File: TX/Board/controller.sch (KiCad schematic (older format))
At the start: 12 parts, among them J1 CONN_SWITCH, J2 PROG_CONN, J3 RX_JMP, J4 TX_JMP, J5 AT_MODE_JUMP, J6 BATT_CONN, J7 GENERIC, U1 ARDUINO_PRO_MINI, U2 ITEAD_HC-05

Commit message: Corrected bugs and added first prototype of receiver board
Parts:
- added R1: R, Resistors_THT:Resistor_Horizontal_RM7mm, symbol R
- J1: value CONN_SWITCH -> PRESENCE_SENS
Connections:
- net +3V3: now also J1.2 (P2)
- net GNDREF: now also R1.2; no longer J1.1 (P1)
- net PRESENCE_SENSOR: now reaches U1.20 (A0)
- net PRESENCE_SENSOR: now also J1.1 (P1), R1.1
- net SWITCH_PRESENZA: no longer names the net of U1.5 (D2)
- net SWITCH_PRESENZA: no longer J1.2 (P2)
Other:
- note added: "AT-MODE jumper"
- note added: "Accellerator\n"
- note added: "Presence sensor\n\n"
- note added: "Programming connector"
- note added: "Programming jumpers"
- note removed: "Acceleratore\n"
- note removed: "Attacco switch \npresenza\n"
- note removed: "Connettore per\nprogrammazione\n"
- note removed: "Jumper per \nprogrammazione\n"
- note removed: "Jumper used for entering AT-MODE\n"
- moved on the sheet: J1
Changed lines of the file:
@@
 encoding utf-8
 Sheet 1 1
-Title "AZUL"
+Title "handy"
 Date "2017-03-29"
-Rev "1"
+Rev "1.1"
 Comp "Matias Fernando Mamone"
 Comment1 ""
@@
 $EndComp
 $Comp
-L GNDREF #PWR01
+L GNDREF #PWR11
 U 1 1 58C7D630
 P 5400 4600
-F 0 "#PWR01" H 5400 4350 50  0001 C CNN
+F 0 "#PWR11" H 5400 4350 50  0001 C CNN
 F 1 "GNDREF" H 5400 4450 50  0000 C CNN
 F 2 "" H 5400 4600 50  0001 C CNN
@@
 $EndComp
 $Comp
-L +3.3V #PWR02
+L +3.3V #PWR10
 U 1 1 58C7D6CB
 P 5400 2050
-F 0 "#PWR02" H 5400 1900 50  0001 C CNN
+F 0 "#PWR10" H 5400 1900 50  0001 C CNN
 F 1 "+3.3V" H 5400 2190 50  0000 C CNN
 F 2 "" H 5400 2050 50  0001 C CNN
@@
 $EndComp
 $Comp
-L +3.3V #PWR03
+L +3.3V #PWR7
 U 1 1 58C7D6EC
-P 3100 1550
-F 0 "#PWR03" H 3100 1400 50  0001 C CNN
-F 1 "+3.3V" H 3100 1690 50  0000 C CNN
-F 2 "" H 3100 1550 50  0001 C CNN
-F 3 "" H 3100 1550 50  0001 C CNN
-	1    3100 1550
+P 3600 1550
+F 0 "#PWR7" H 3600 1400 50  0001 C CNN
+F 1 "+3.3V" H 3600 1690 50  0000 C CNN
+F 2 "" H 3600 1550 50  0001 C CNN
+F 3 "" H 3600 1550 50  0001 C CNN
+	1    3600 1550
 	1    0    0    -1
 $EndComp
 $Comp
-L GNDREF #PWR04
+L GNDREF #PWR6
 U 1 1 58C7D7DC
-P 3850 2450
-F 0 "#PWR04" H 3850 2200 50  0001 C CNN
-F 1 "GNDREF" H 3850 2300 50  0000 C CNN
-F 2 "" H 3850 2450 50  0001 C CNN
-F 3 "" H 3850 2450 50  0001 C CNN
-	1    3850 2450
+P 3350 2700
+F 0 "#PWR6" H 3350 2450 50  0001 C CNN
+F 1 "GNDREF" H 3350 2550 50  0000 C CNN
+F 2 "" H 3350 2700 50  0001 C CNN
+F 3 "" H 3350 2700 50  0001 C CNN
+	1    3350 2700
 	1    0    0    -1
 $EndComp
@@
 $EndComp
 $Comp
-L GNDREF #PWR05
+L GNDREF #PWR8
 U 1 1 58C7E1D0
 P 4200 7350
-F 0 "#PWR05" H 4200 7100 50  0001 C CNN
+F 0 "#PWR8" H 4200 7100 50  0001 C CNN
 F 1 "GNDREF" H 4200 7200 50  0000 C CNN
 F 2 "" H 4200 7350 50  0001 C CNN
@@
 $EndComp
 $Comp
-L +3.3V #PWR06
+L +3.3V #PWR9
 U 1 1 58C7E222
 P 4500 6400
-F 0 "#PWR06" H 4500 6250 50  0001 C CNN
+F 0 "#PWR9" H 4500 6250 50  0001 C CNN
 F 1 "+3.3V" H 4500 6540 50  0000 C CNN
 F 2 "" H 4500 6400 50  0001 C CNN
@@
 $EndComp
 $Comp
-L GNDREF #PWR07
+L GNDREF #PWR4
 U 1 1 58C7E432
 P 2600 7350
-F 0 "#PWR07" H 2600 7100 50  0001 C CNN
+F 0 "#PWR4" H 2600 7100 50  0001 C CNN
 F 1 "GNDREF" H 2600 7200 50  0000 C CNN
 F 2 "" H 2600 7350 50  0001 C CNN
@@
 $EndComp
 $Comp
-L +3.3V #PWR08
+L +3.3V #PWR3
 U 1 1 58C7E455
 P 2600 6950
-F 0 "#PWR08" H 2600 6800 50  0001 C CNN
+F 0 "#PWR3" H 2600 6800 50  0001 C CNN
 F 1 "+3.3V" H 2600 7090 50  0000 C CNN
 F 2 "" H 2600 6950 50  0001 C CNN
@@
 ACCEL_POT
 Text Notes 2600 6700 0    60   ~ 0
-Acceleratore\n
+Accellerator\n
 Text Notes 5800 6350 0    60   ~ 0
-Jumper per \nprogrammazione\n
+Programming jumpers
 Text Notes 3800 6200 0    60   ~ 0
-Connettore per\nprogrammazione\n
-Text GLabel 1550 3100 0    60   Input ~ 0
-SWITCH_PRESENZA
+Programming connector
 $Comp
 L CONN_01X02 J1
 U 1 1 58C7EEA4
-P 1150 6750
-F 0 "J1" H 1150 6900 50  0000 C CNN
-F 1 "CONN_SWITCH" V 1250 6750 50  0000 C CNN
-F 2 "Pin_Headers:Pin_Header_Straight_1x02" H 1150 6750 50  0001 C CNN
-F 3 "" H 1150 6750 50  0001 C CNN
-	1    1150 6750
-	0    -1   -1   0
-$EndComp
-$Comp
-L GNDREF #PWR09
-U 1 1 58C7EEE7
-P 1100 7400
-F 0 "#PWR09" H 1100 7150 50  0001 C CNN
-F 1 "GNDREF" H 1100 7250 50  0000 C CNN
-F 2 "" H 1100 7400 50  0001 C CNN
-F 3 "" H 1100 7400 50  0001 C CNN
-	1    1100 7400
-	1    0    0    -1
+P 1100 6850
+F 0 "J1" H 1100 7000 50  0000 C CNN
+F 1 "PRESENCE_SENS" V 1200 6850 50  0000 C CNN
+F 2 "Pin_Headers:Pin_Header_Straight_1x02" H 1100 6850 50  0001 C CNN
+F 3 "" H 1100 6850 50  0001 C CNN
+	1    1100 6850
+	-1   0    0    1
 $EndComp
-Text GLabel 1250 7200 2    60   Input ~ 0
-SWITCH_PRESENZA
-Text Notes 1200 6550 0    60   ~ 0
-Attacco switch \npresenza\n
+Text Notes 1150 6550 0    60   ~ 0
+Presence sensor\n\n
 Text GLabel 4600 2850 0    60   Input ~ 0
 TX_BT
@@
 AT_MODE
 $Comp
-L +3.3V #PWR010
+L +3.3V #PWR15
 U 1 1 58D52A1F
 P 9750 1150
-F 0 "#PWR010" H 9750 1000 50  0001 C CNN
+F 0 "#PWR15" H 9750 1000 50  0001 C CNN
 F 1 "+3.3V" H 9750 1290 50  0000 C CNN
 F 2 "" H 9750 1150 50  0001 C CNN
@@
 $EndComp
 $Comp
-L +BATT #PWR011
+L +BATT #PWR5
 U 1 1 58D52B9C
-P 3200 2500
-F 0 "#PWR011" H 3200 2350 50  0001 C CNN
-F 1 "+BATT" H 3200 2640 50  0000 C CNN
-F 2 "" H 3200 2500 50  0001 C CNN
-F 3 "" H 3200 2500 50  0001 C CNN
-	1    3200 2500
+P 3000 2550
+F 0 "#PWR5" H 3000 2400 50  0001 C CNN
+F 1 "+BATT" H 3000 2690 50  0000 C CNN
+F 2 "" H 3000 2550 50  0001 C CNN
+F 3 "" H 3000 2550 50  0001 C CNN
+	1    3000 2550
 	1    0    0    -1
 $EndComp
@@
 $EndComp
 $Comp
-L +BATT #PWR012
+L +BATT #PWR16
 U 1 1 58D52CB9
 P 10750 2100
-F 0 "#PWR012" H 10750 1950 50  0001 C CNN
+F 0 "#PWR16" H 10750 1950 50  0001 C CNN
 F 1 "+BATT" H 10750 2240 50  0000 C CNN
 F 2 "" H 10750 2100 50  0001 C CNN
@@
 $EndComp
 $Comp
-L GNDREF #PWR013
+L GNDREF #PWR17
 U 1 1 58D52DB0
 P 10750 2650
-F 0 "#PWR013" H 10750 2400 50  0001 C CNN
+F 0 "#PWR17" H 10750 2400 50  0001 C CNN
 F 1 "GNDREF" H 10750 2500 50  0000 C CNN
 F 2 "" H 10750 2650 50  0001 C CNN
@@
 	1    0    0    -1
 $EndComp
-Text Notes 9450 750  0    60   ~ 0
-Jumper used for entering AT-MODE\n
+Text Notes 9950 750  0    60   ~ 0
+AT-MODE jumper
 Text Notes 10400 1850 0    60   ~ 0
 Battery\nconnector\n
@@
 $EndComp
 $Comp
-L +BATT #PWR014
+L +BATT #PWR13
 U 1 1 58D535FE
 P 9250 3450
-F 0 "#PWR014" H 9250 3300 50  0001 C CNN
+F 0 "#PWR13" H 9250 3300 50  0001 C CNN
 F 1 "+BATT" H 9250 3590 50  0000 C CNN
 F 2 "" H 9250 3450 50  0001 C CNN
@@
 $EndComp
 $Comp
-L GNDREF #PWR015
+L GNDREF #PWR14
 U 1 1 58D53630
 P 9250 4750
-F 0 "#PWR015" H 9250 4500 50  0001 C CNN
+F 0 "#PWR14" H 9250 4500 50  0001 C CNN
 F 1 "GNDREF" H 9250 4600 50  0000 C CNN
 F 2 "" H 9250 4750 50  0001 C CNN
@@
 $EndComp
 $Comp
-L GNDREF #PWR016
+L GNDREF #PWR12
 U 1 1 58D58378
 P 9050 6200
-F 0 "#PWR016" H 9050 5950 50  0001 C CNN
+F 0 "#PWR12" H 9050 5950 50  0001 C CNN
 F 1 "GNDREF" H 9050 6050 50  0000 C CNN
 F 2 "" H 9050 6200 50  0001 C CNN
@@
 	10650 2450 10750 2450
 Wire Wire Line
-	3200 2700 3200 2500
+	3000 2700 3000 2550
 Wire Wire Line
-	2950 2700 3200 2700
+	2950 2700 3000 2700
 Wire Wire Line
 	9750 1450 9750 1150
@@
 Wire Notes Line
 	2200 7650 2200 6300
-Wire Wire Line
-	1200 7200 1250 7200
-Wire Wire Line
-	1200 6950 1200 7200
-Wire Wire Line
-	1100 7400 1100 6950
 Wire Notes Line
 	3550 5850 3550 7650
@@
 Wire Wire Line
 	3250 3100 2950 3100
-Connection ~ 3500 2150
-Wire Wire Line
-	3850 2150 3850 2450
 Wire Wire Line
-	3500 2150 3500 2800
-Wire Wire Line
-	3500 2800 2950 2800
+	3200 2800 2950 2800
 Wire Wire Line
 	2600 7350 2600 7300
@@
 Wire Wire Line
 	6450 7450 6250 7450
-Connection ~ 3100 2050
+Connection ~ 3600 2050
 Wire Wire Line
-	3100 1550 3100 3000
+	3600 1550 3600 3000
 Wire Wire Line
-	3100 3000 2950 3000
+	3600 3000 2950 3000
 Wire Wire Line
-	2350 2050 3100 2050
+	3600 2050 2350 2050
 Wire Wire Line
-	2350 2250 2350 2050
+	2350 2050 2350 2250
 Connection ~ 2550 2150
 Wire Wire Line
 	2550 2150 2550 2250
 Wire Wire Line
-	2450 2150 3850 2150
+	2450 2150 3200 2150
 Wire Wire Line
 	2450 2250 2450 2150
@@
 NoConn ~ 2600 4200
 NoConn ~ 2950 2900
-Wire Wire Line
-	1550 3100 1700 3100
 Text GLabel 3250 3300 2    60   Input ~ 0
 AT_MODE
-NoConn ~ 2950 3400
 NoConn ~ 2950 3500
 NoConn ~ 1700 3200
 Wire Wire Line
 	3250 3300 2950 3300
+$Comp
+L R R1
+U 1 1 58E0B656
+P 1500 7200
+F 0 "R1" V 1580 7200 50  0000 C CNN
+F 1 "R" V 1500 7200 50  0000 C CNN
+F 2 "Resistors_THT:Resistor_Horizontal_RM7mm" V 1430 7200 50  0001 C CNN
+F 3 "" H 1500 7200 50  0001 C CNN
+	1    1500 7200
+	1    0    0    -1
+$EndComp
+$Comp
+L +3.3V #PWR1
+U 1 1 58E0B708
+P 1500 6700
+F 0 "#PWR1" H 1500 6550 50  0001 C CNN
+F 1 "+3.3V" H 1500 6840 50  0000 C CNN
+F 2 "" H 1500 6700 50  0001 C CNN
+F 3 "" H 1500 6700 50  0001 C CNN
+	1    1500 6700
+	1    0    0    -1
+$EndComp
+Wire Wire Line
+	1300 6900 1700 6900
+Wire Wire Line
+	1500 6900 1500 7050
+Wire Wire Line
+	1300 6800 1500 6800
+Wire Wire Line
+	1500 6800 1500 6700
+$Comp
+L GNDREF #PWR2
+U 1 1 58E0B866
+P 1500 7450
+F 0 "#PWR2" H 1500 7200 50  0001 C CNN
+F 1 "GNDREF" H 1500 7300 50  0000 C CNN
+F 2 "" H 1500 7450 50  0001 C CNN
+F 3 "" H 1500 7450 50  0001 C CNN
+	1    1500 7450
+	1    0    0    -1
+$EndComp
+Wire Wire Line
+	1500 7450 1500 7350
+Text GLabel 1700 6900 2    60   Input ~ 0
+PRESENCE_SENSOR
+Connection ~ 1500 6900
+Text GLabel 3250 3400 2    60   Input ~ 0
+PRESENCE_SENSOR
+Wire Wire Line
+	3250 3400 2950 3400
+NoConn ~ 1700 3100
+Wire Wire Line
+	3200 2150 3200 2800
+Wire Wire Line
+	3200 2600 3350 2600
+Wire Wire Line
+	3350 2600 3350 2700
+Connection ~ 3200 2600
 $EndSCHEMATC

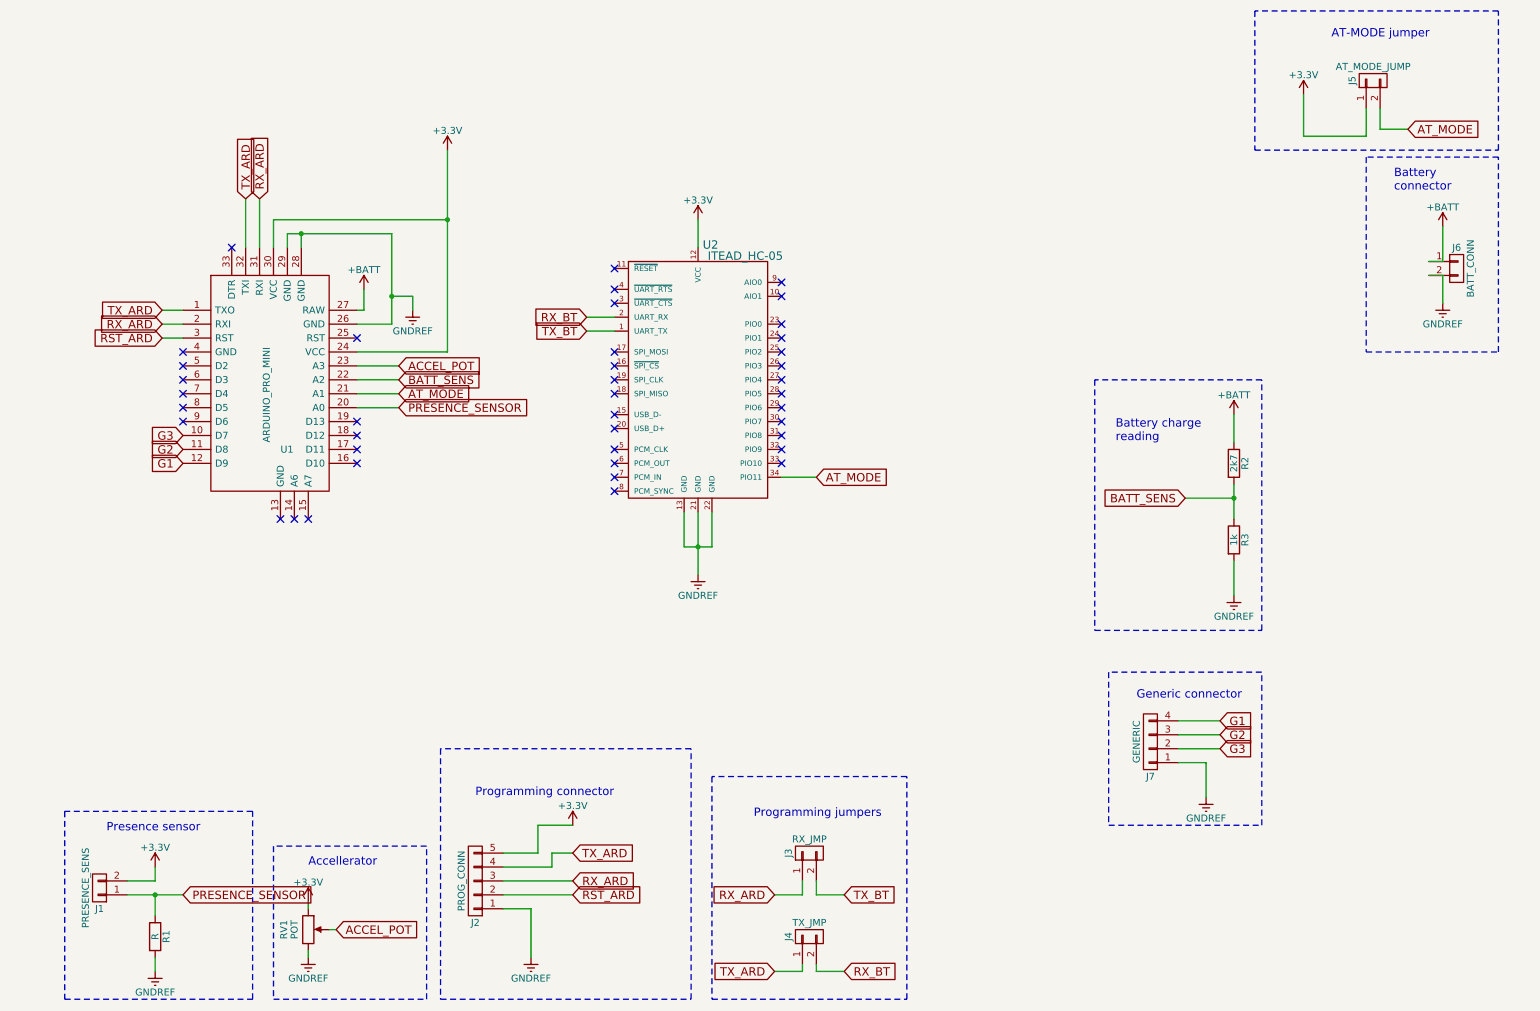
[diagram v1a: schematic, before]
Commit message: Added low-pass filter to the transmitter -> stable acc reading
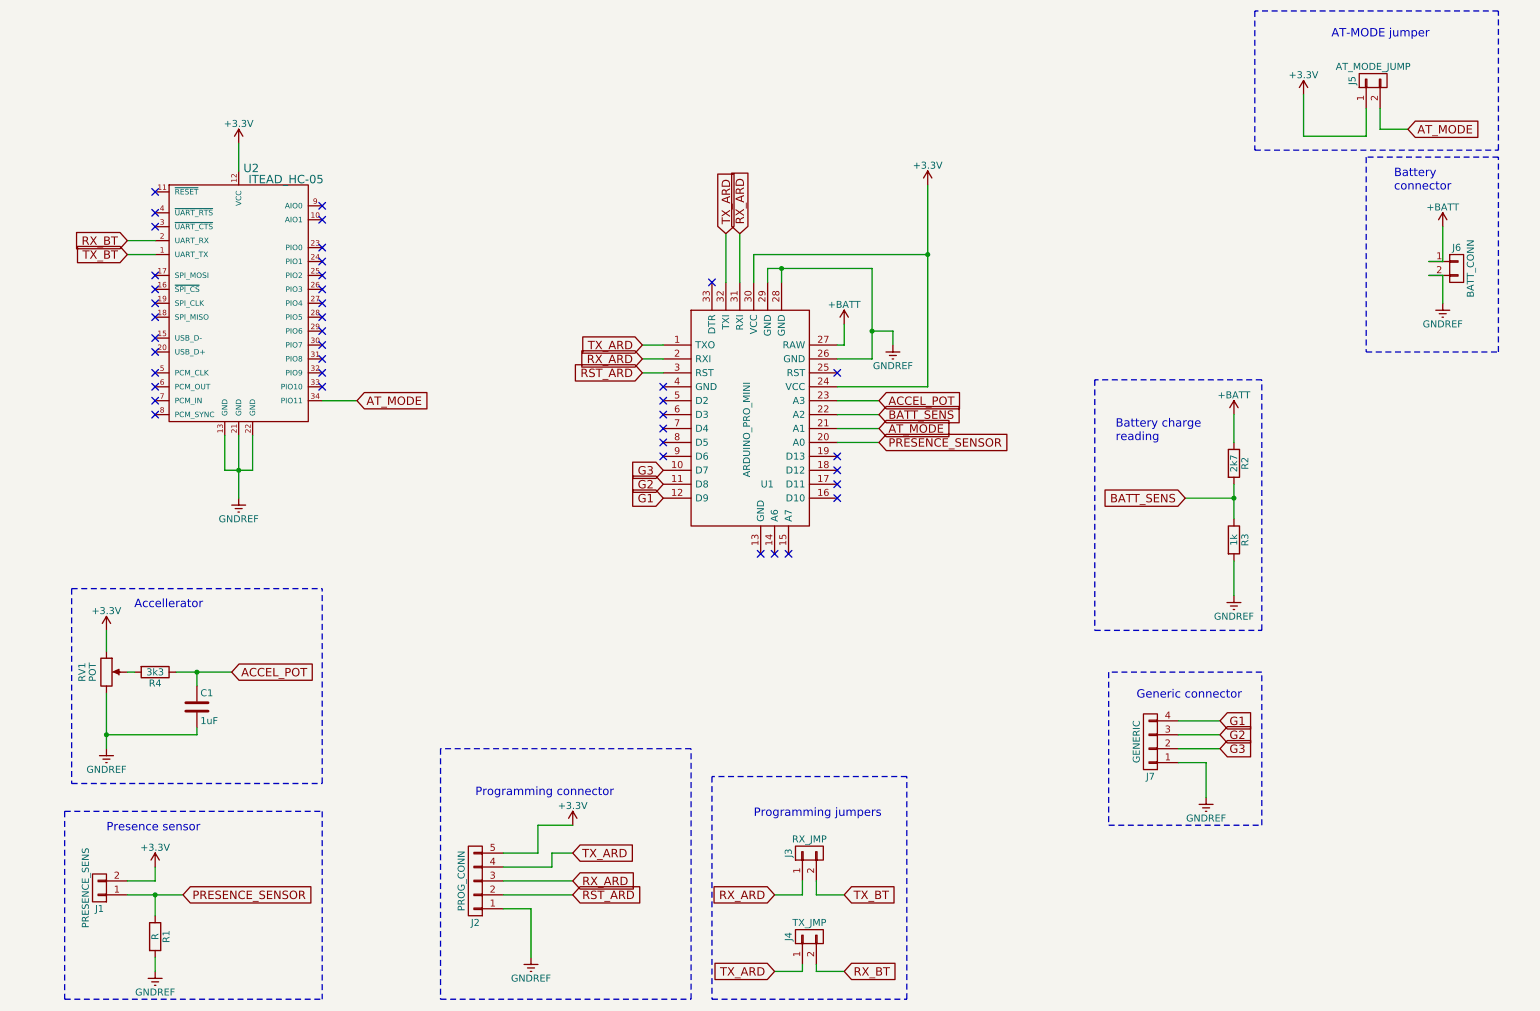
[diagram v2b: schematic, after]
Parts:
- added C1: 1uF, Capacitors_THT:C_Rect_L4_W2.5_P2.5, symbol C
- added R4: 3k3, Resistors_THT:Resistor_Horizontal_RM7mm, symbol R
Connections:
- net ACCEL_POT: now also C1.1, R4.1; no longer RV1.2
- net GNDREF: now also C1.2
- new net: R4.2, RV1.2
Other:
- moved on the sheet: RV1, U1, U2
